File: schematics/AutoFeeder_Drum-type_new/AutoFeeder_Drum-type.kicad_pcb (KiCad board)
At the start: 2 copper layers, 65.5 x 80 mm, 27 parts, among them J1 USB_C_Receptacle_6, J3 Conn_01x05, J4 Conn_02x02_Odd_Even, M1 Motor_DC, U2 NJL5901AR-1, U3 PIC16F1705-I/SO, U4 ZXBM5210-S, U6 NJL5901AR-1

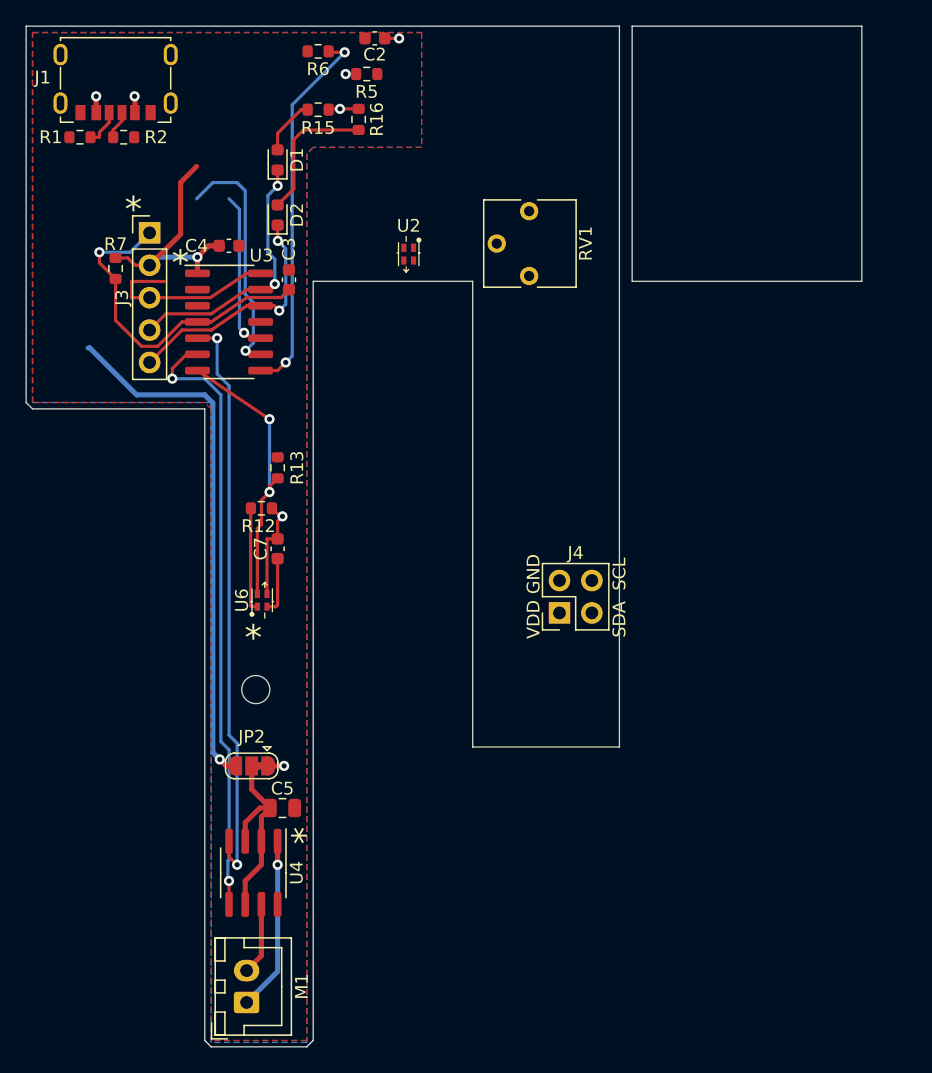
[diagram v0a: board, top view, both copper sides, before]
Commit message: Test reading/writing from/to HEF-block
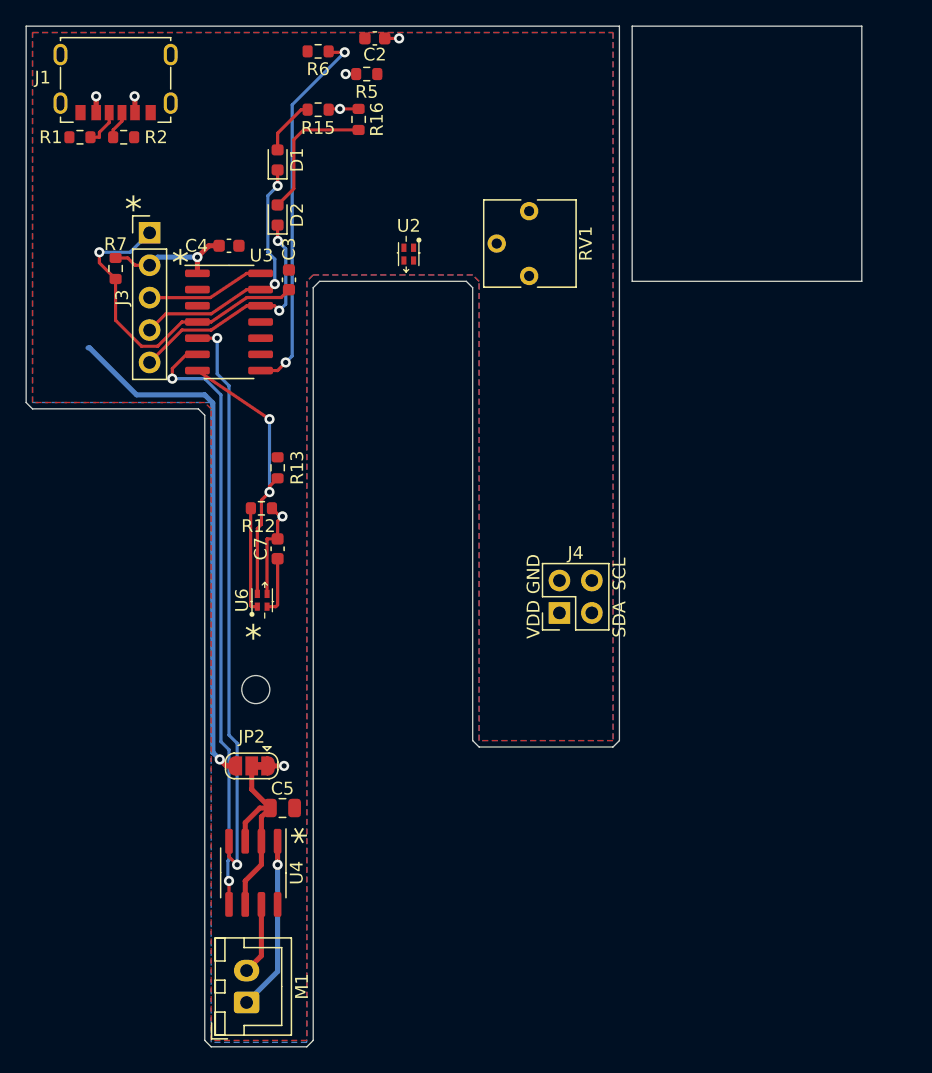
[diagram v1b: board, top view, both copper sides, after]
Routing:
- net /SDA: track 18.9 -> 0.00 mm, vias 1 -> 0
- net /SCL: track 12.4 -> 0.00 mm, vias 1 -> 0
- net +5V: track 35.8 -> 26.6 mm
- net GND: track 19.0 -> 13.8 mm
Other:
- outline, holes or cut-outs redrawn
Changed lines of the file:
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@@
     )
   )
-  (gr_line (start 137.16 81.28) (end 137.16 88.9) (layer "B.SilkS") (width 0.15))
-  (gr_line (start 137.16 88.9) (end 142.875 88.9) (layer "B.SilkS") (width 0.15))
-  (gr_line (start 142.875 81.28) (end 137.16 81.28) (layer "B.SilkS") (width 0.15))
-  (gr_line (start 142.875 88.9) (end 142.875 81.28) (layer "B.SilkS") (width 0.15))
   (gr_line (start 184 80) (end 184 60) (layer "Edge.Cuts") (width 0.1))
+  (gr_line (start 171.5 116) (end 172 116.5) (layer "Edge.Cuts") (width 0.1))
   (gr_line (start 136.5 60) (end 183 60) (layer "Edge.Cuts") (width 0.1))
-  (gr_line (start 171.5 80) (end 171.5 116.5) (layer "Edge.Cuts") (width 0.1))
-  (gr_line (start 183 60) (end 183 116.5) (layer "Edge.Cuts") (width 0.1))
-  (gr_line (start 159 80) (end 159 139.5) (layer "Edge.Cuts") (width 0.1))
-  (gr_line (start 137 90) (end 150.5 90) (layer "Edge.Cuts") (width 0.1))
-  (gr_line (start 171.5 80) (end 159 80) (layer "Edge.Cuts") (width 0.1))
+  (gr_line (start 171.5 80.5) (end 171.5 116) (layer "Edge.Cuts") (width 0.1))
+  (gr_line (start 183 60) (end 183 116) (layer "Edge.Cuts") (width 0.1))
+  (gr_line (start 159 80.5) (end 159 139.5) (layer "Edge.Cuts") (width 0.1))
+  (gr_line (start 171 80) (end 171.5 80.5) (layer "Edge.Cuts") (width 0.1))
+  (gr_line (start 137 90) (end 150 90) (layer "Edge.Cuts") (width 0.1))
+  (gr_line (start 171 80) (end 159.5 80) (layer "Edge.Cuts") (width 0.1))
   (gr_line (start 150.5 139.5) (end 151 140) (layer "Edge.Cuts") (width 0.1))
   (gr_line (start 202 60) (end 202 80) (layer "Edge.Cuts") (width 0.1))
@@
   (gr_line (start 151 140) (end 158.5 140) (layer "Edge.Cuts") (width 0.1))
   (gr_line (start 202 80) (end 184 80) (layer "Edge.Cuts") (width 0.1))
-  (gr_line (start 150.5 90) (end 150.5 139.5) (layer "Edge.Cuts") (width 0.1))
+  (gr_line (start 150 90) (end 150.5 90.5) (layer "Edge.Cuts") (width 0.1))
+  (gr_line (start 150.5 90.5) (end 150.5 139.5) (layer "Edge.Cuts") (width 0.1))
+  (gr_line (start 159.5 80) (end 159 80.5) (layer "Edge.Cuts") (width 0.1))
   (gr_line (start 136.5 89.5) (end 137 90) (layer "Edge.Cuts") (width 0.1))
-  (gr_line (start 171.5 116.5) (end 183 116.5) (layer "Edge.Cuts") (width 0.1))
+  (gr_line (start 172 116.5) (end 182.5 116.5) (layer "Edge.Cuts") (width 0.1))
   (gr_line (start 184 60) (end 202 60) (layer "Edge.Cuts") (width 0.1))
   (gr_line (start 136.5 60) (end 136.5 89.5) (layer "Edge.Cuts") (width 0.1))
+  (gr_line (start 182.5 116.5) (end 183 116) (layer "Edge.Cuts") (width 0.1))
   (gr_text "GND" (at 147.32 81.28) (layer "B.SilkS")
     (effects (font (size 1 1) (thickness 0.15)) (justify right mirror))
@@
     (style (thickness 0.15) (arrow_length 1.27) (text_position_mode 0) (extension_height 0.58642) (extension_offset 0.5) keep_text_aligned)
   )
-  (segment (start 144.78 81.28) (end 144.78 80.01) (width 0.25) (layer "F.Cu") (net 1))
   (segment (start 150.936751 81.28) (end 153.797 79.375) (width 0.25) (layer "F.Cu") (net 1))
-  (segment (start 144.78 80.01) (end 147.32 80.01) (width 0.25) (layer "F.Cu") (net 1))
   (segment (start 156.0675 105.5) (end 156.21 105.3575) (width 0.25) (layer "F.Cu") (net 1))
-  (segment (start 146.177 81.28) (end 144.78 81.28) (width 0.25) (layer "F.Cu") (net 1))
   (segment (start 155.38 105.5) (end 156.0675 105.5) (width 0.25) (layer "F.Cu") (net 1))
   (segment (start 153.797 79.375) (end 154.875 79.375) (width 0.25) (layer "F.Cu") (net 1))
@@
   (segment (start 156.4 98.425) (end 155.765 97.79) (width 0.25) (layer "F.Cu") (net 2))
   (segment (start 156.718 117.983) (end 155.478 117.983) (width 0.4) (layer "F.Cu") (net 2))
-  (segment (start 146.177 78.74) (end 148.61 76.307) (width 0.4) (layer "F.Cu") (net 2))
   (segment (start 144.463 78.169) (end 145.034 78.74) (width 0.25) (layer "F.Cu") (net 2))
   (segment (start 160.273 66.485) (end 160.21 66.548) (width 0.25) (layer "F.Cu") (net 2))
   (segment (start 156.591 98.425) (end 156.4 98.425) (width 0.25) (layer "F.Cu") (net 2))
-  (segment (start 148.61 72.243) (end 149.86 70.993) (width 0.4) (layer "F.Cu") (net 2))
   (segment (start 145 65.5) (end 145.03 65.53) (width 0.4) (layer "F.Cu") (net 2))
   (segment (start 156.21 100.19) (end 155.38 100.19) (width 0.25) (layer "F.Cu") (net 2))
   (segment (start 145.034 78.74) (end 146.177 78.74) (width 0.25) (layer "F.Cu") (net 2))
   (segment (start 155.38 100.19) (end 155.38 104.5) (width 0.25) (layer "F.Cu") (net 2))
-  (segment (start 148.61 76.307) (end 148.61 72.243) (width 0.4) (layer "F.Cu") (net 2))
   (segment (start 149.925 78.105) (end 149.925 79.375) (width 0.4) (layer "F.Cu") (net 2))
   (segment (start 156.591 98.425) (end 156.21 98.806) (width 0.25) (layer "F.Cu") (net 2))
@@
   (segment (start 152.4005 116.7135) (end 152.4005 125.339195) (width 0.25) (layer "B.Cu") (net 11))
   (segment (start 151.765 116.078) (end 152.4005 116.7135) (width 0.25) (layer "B.Cu") (net 11))
-  (segment (start 153.580202 84.036798) (end 154.051 84.455) (width 0.25) (layer "F.Cu") (net 12))
-  (segment (start 154.051 84.455) (end 154.875 84.455) (width 0.25) (layer "F.Cu") (net 12))
-  (via (at 153.580202 84.036798) (size 0.8) (drill 0.4) (layers "F.Cu" "B.Cu") (net 12))
-  (segment (start 153.22 83.676596) (end 153.580202 84.036798) (width 0.25) (layer "B.Cu") (net 12))
-  (segment (start 153.22 74.353) (end 153.22 83.676596) (width 0.25) (layer "B.Cu") (net 12))
-  (segment (start 152.4 73.533) (end 153.22 74.353) (width 0.25) (layer "B.Cu") (net 12))
-  (segment (start 154.137896 85.725) (end 154.875 85.725) (width 0.25) (layer "F.Cu") (net 13))
-  (segment (start 153.697836 85.443164) (end 154.137896 85.725) (width 0.25) (layer "F.Cu") (net 13))
-  (via (at 153.697836 85.443164) (size 0.8) (drill 0.4) (layers "F.Cu" "B.Cu") (net 13))
-  (segment (start 154.305202 84.835798) (end 154.305202 81.661202) (width 0.25) (layer "B.Cu") (net 13))
-  (segment (start 153.67 81.026) (end 153.67 72.898) (width 0.25) (layer "B.Cu") (net 13))
-  (segment (start 153.035 72.263) (end 151.13 72.263) (width 0.25) (layer "B.Cu") (net 13))
-  (segment (start 153.67 72.898) (end 153.035 72.263) (width 0.25) (layer "B.Cu") (net 13))
-  (segment (start 153.697836 85.443164) (end 154.305202 84.835798) (width 0.25) (layer "B.Cu") (net 13))
-  (segment (start 154.305202 81.661202) (end 153.67 81.026) (width 0.25) (layer "B.Cu") (net 13))
-  (segment (start 151.13 72.263) (end 149.86 73.533) (width 0.25) (layer "B.Cu") (net 13))
   (segment (start 154.095 97.81) (end 154.115 97.79) (width 0.25) (layer "F.Cu") (net 14))
   (segment (start 154.095 105.41) (end 154.095 97.81) (width 0.25) (layer "F.Cu") (net 14))
@@
     (connect_pads (clearance 0.508))
     (min_thickness 0.254) (filled_areas_thickness no)
-    (fill yes (thermal_gap 0.508) (thermal_bridge_width 0.508))
+    (fill (thermal_gap 0.508) (thermal_bridge_width 0.508))
     (polygon
       (pts
-        (xy 167.5 69.5)
-        (xy 159 69.5)
-        (xy 158.5 70)
+        (xy 182.5 116)
+        (xy 172 116)
+        (xy 172 80)
+        (xy 171.5 79.5)
+        (xy 159 79.5)
+        (xy 158.5 80)
         (xy 158.5 139.5)
         (xy 151 139.5)
@@
         (xy 137 89.5)
         (xy 137 60.5)
-        (xy 167.5 60.5)
+        (xy 182.5 60.5)
       )
     )
@@
     (connect_pads (clearance 0.508))
     (min_thickness 0.254) (filled_areas_thickness no)
-    (fill yes (thermal_gap 0.508) (thermal_bridge_width 0.508))
+    (fill (thermal_gap 0.508) (thermal_bridge_width 0.508))
     (polygon
       (pts
-        (xy 167.5 69.5)
-        (xy 159 69.5)
-        (xy 158.5 70)
+        (xy 182.5 116)
+        (xy 172 116)
+        (xy 172 80)
+        (xy 171.5 79.5)
+        (xy 159 79.5)
+        (xy 158.5 80)
         (xy 158.5 139.65)
         (xy 151 139.65)
@@
         (xy 137 89.5)
         (xy 137 60.5)
-        (xy 167.5 60.5)
+        (xy 182.5 60.5)
       )
     )

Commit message: Rev.02: Rev01 had a problem with the deep feeder hitting the PCB. Rev02 avoided this problem by overlapping two PCBs for the sensor section.; Three sensitivity options are available for white, transparent, and black feeders.
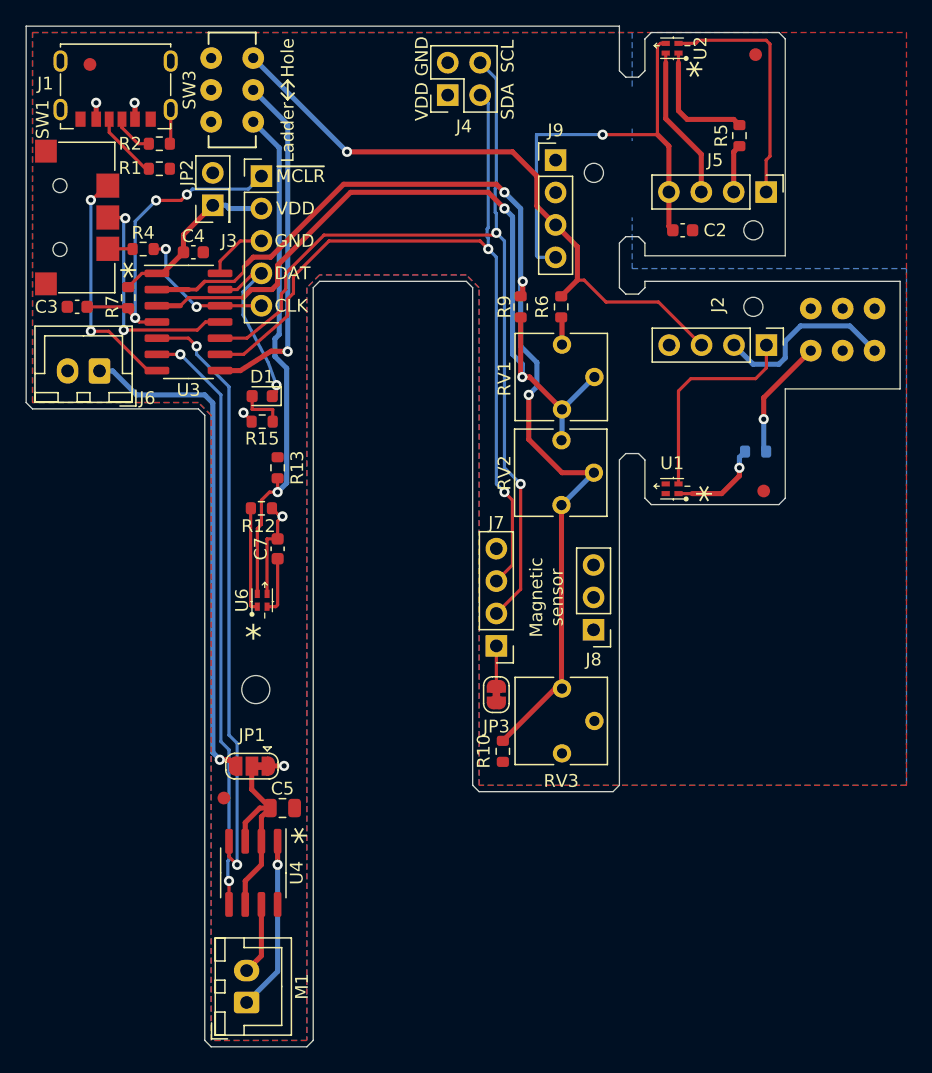
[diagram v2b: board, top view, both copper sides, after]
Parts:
- removed D2: LED, LED_SMD:LED_0603_1608Metric
- removed R16: 1k, Resistor_SMD:R_0603_1608Metric
- added ?: , , F.Cu at (194.3, 96.4)
- added ?: , , F.Cu at (193.7, 62.2)
- added ?: , , F.Cu at (141.5, 63.0)
- added J2: Conn_01x04, Connector_PinHeader_2.54mm:PinHeader_1x04_P2.54mm_Vertical, F.Cu at (194.5, 85.0)
- added J5: Conn_01x04, Connector_PinHeader_2.54mm:PinHeader_1x04_P2.54mm_Vertical, F.Cu at (194.5, 73.0)
- added J6: Conn_01x02, Connector_JST:JST_XH_B2B-XH-A_1x02_P2.50mm_Vertical, F.Cu at (142.2, 87.0)
- added J7: Conn_01x04, Connector_PinHeader_2.54mm:PinHeader_1x04_P2.54mm_Vertical, F.Cu at (173.4, 108.6)
- added J8: Conn_01x03, Connector_PinHeader_2.54mm:PinHeader_1x03_P2.54mm_Vertical, F.Cu at (181.0, 107.3)
- added J9: Conn_01x04, Connector_PinHeader_2.54mm:PinHeader_1x04_P2.54mm_Vertical, F.Cu at (178.0, 70.5)
- added JP1: SolderJumper, Jumper:SolderJumper-3_P1.3mm_Bridged12_RoundedPad1.0x1.5mm, F.Cu at (154.2, 118.0)
- added JP3: Jumper_2_Bridged, Jumper:SolderJumper-2_P1.3mm_Bridged_RoundedPad1.0x1.5mm, F.Cu at (173.4, 112.4)
- added R10: 18k, Resistor_SMD:R_0603_1608Metric, F.Cu at (173.9, 116.8)
- added R4: 1k, Resistor_SMD:R_0603_1608Metric, F.Cu at (145.7, 77.5)
- added R8: 510, Resistor_SMD:R_0603_1608Metric, B.Cu at (193.7, 93.3)
- added R9: 10k, Resistor_SMD:R_0603_1608Metric, F.Cu at (175.3, 82.0)
- added REF**: DrillHoleOval2x2, mylib:DrillHoleOval2.5x8mm, F.Cu at (181.0, 71.5)
- added REF**: DrillHoleOval2x2, mylib:DrillHoleOval2.5x8mm, F.Cu at (193.5, 76.0)
- added REF**: DrillHoleOval2x4, mylib:DrillHoleOval2.5x8mm, F.Cu at (170.0, 75.0)
- added REF**: DrillHoleOval2x6, mylib:DrillHoleOval2.5x8mm, F.Cu at (184.0, 85.0)
- added REF**: DrillHoleOval2x4, mylib:DrillHoleOval2.5x8mm, F.Cu at (184.0, 66.5)
- added REF**: DrillHoleOval2x4, mylib:DrillHoleOval2.5x8mm, F.Cu at (190.5, 65.0)
- added REF**: Fiducial_1mm_Mask2mm, Fiducial:Fiducial_1mm_Mask2mm, F.Cu at (152.0, 120.5)
- added REF**: DrillHoleOval2x6, mylib:DrillHoleOval2.5x8mm, F.Cu at (190.0, 92.7)
- added REF**: DrillHoleOval2x2, mylib:DrillHoleOval2.5x8mm, F.Cu at (193.5, 82.0)
- added REF**: DrillHoleOval2.5x8mm, mylib:DrillHoleOval2.5x8mm, F.Cu at (184.0, 72.0)
- added REF**: DrillHoleOval2x3, mylib:DrillHoleOval2.5x8mm, F.Cu at (184.0, 91.0)
- added RV2: 20k, Potentiometer_THT:Potentiometer_Vishay_T73YP_Vertical, F.Cu at (178.5, 97.5)
- added RV3: 20k, Potentiometer_THT:Potentiometer_Vishay_T73YP_Vertical, F.Cu at (178.5, 117.0)
- added SW1: SW_SPDT_AND_Push, mylib:THMU26_2, F.Cu at (139.3, 75.0)
- added SW2: IS-2235, mylib:Slide-SW-IS-2235, B.Cu at (198.0, 85.4)
- added SW3: IS-2235, mylib:Slide-SW-IS-2235, F.Cu at (154.3, 62.5)
- added U1: NJL5901AR-1, mylib:NJL5901AR-1, F.Cu at (187.1, 96.3)
- JP2: value SolderJumper -> Jumper_2_Bridged; footprint Jumper:SolderJumper-3_P1.3mm_Bridged12_RoundedPad1.0x1.5mm -> Connector_PinHeader_2.54mm:PinHeader_2x01_P2.54mm_Vertical
- R5: value 820 -> 510
- RV1: value 50k -> 1k
- moved JP2 44.0 mm to (151.1, 74.0), turned to 90 degrees
- moved J4 41.5 mm to (169.5, 65.4)
- moved R5 29.6 mm to (192.4, 68.6), turned to 90 degrees
- moved C2 28.4 mm to (188.0, 76.0), turned to 0 degrees
- moved R6 27.6 mm to (178.4, 82.0), turned to -90 degrees
- moved U2 26.2 mm to (187.1, 61.7), turned to 0 degrees
- moved R15 24.8 mm to (155.0, 91.0), turned to 0 degrees
- moved D1 18.6 mm to (155.0, 89.0), turned to 180 degrees
- moved C3 16.7 mm to (140.5, 82.0), turned to 180 degrees
- moved RV1 15.8 mm to (178.5, 90.0), turned to 0 degrees
- moved J3 9.83 mm to (154.9, 71.8)
- moved R1 6.69 mm to (146.9, 71.2), turned to 0 degrees
- moved U3 3.18 mm to (149.2, 83.2)
- moved C4 2.84 mm to (149.6, 77.7)
- moved R2 2.84 mm to (146.9, 69.2)
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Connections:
- net Net-(D2-Pad1) renamed /CCW
- C4 pad 2: +5V -> Net-(C4-Pad2)
- J3 pad 2: +5V -> Net-(C4-Pad2)
- JP2 pad 1: +5V -> Net-(C4-Pad2)
- JP2 pad 2: Net-(C5-Pad1) -> +5V
- R5 pad 1: +5V -> /IR_DOWN
- R7 pad 2: +5V -> Net-(C4-Pad2)
- RV1 pad 1: Net-(R6-Pad2) -> /RA4
- RV1 pad 2: GND -> /RA4
- RV1 pad 3: GND -> Net-(R6-Pad2)
- U2 pad 4: /Sensor0 -> Net-(J5-Pad3)
- U3 pad 1: +5V -> Net-(C4-Pad2)
- U3 pad 2: /Sw1 -> /RA5
- U3 pad 7: /Sensor1 -> /CW
- U3 pad 8: /Sensor0 -> Net-(SW3-Pad2)
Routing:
- net /RA5: track 0.00 -> 83.7 mm, vias 0 -> 3
- net /SCL: track 0.00 -> 71.8 mm, vias 0 -> 2
- net /SDA: track 0.00 -> 66.1 mm, vias 0 -> 2
- net /RA4: track 0.00 -> 61.0 mm, vias 0 -> 2
- net /VM: track 41.1 -> 0.00 mm, vias 1 -> 0
- net Net-(J6-Pad1): track 0.00 -> 39.5 mm, vias 0 -> 1
- net GND: track 13.8 -> 47.9 mm
- net Net-(SW3-Pad2): track 0.00 -> 27.4 mm, vias 0 -> 1
- net +5V: track 26.6 -> 49.2 mm, vias 8 -> 6
- net /Sensor0: track 29.7 -> 49.2 mm, vias 2 -> 1
- net /CW: track 0.00 -> 18.6 mm, vias 0 -> 2
- net /Sensor1: track 22.2 -> 40.8 mm, vias 2 -> 1
- net /RA2: track 0.00 -> 18.0 mm, vias 0 -> 2
- net Net-(J2-Pad2): track 0.00 -> 14.4 mm
- net Net-(C4-Pad2): track 0.00 -> 14.0 mm
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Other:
- board size 65.5 x 80 mm -> 68.5 x 80 mm
- board text added: "0.25mm Not required"
- board text added: "Hole"
- board text added: "Ladder"
- board text added: "Lower"
- board text added: "Magnetic sensor"
- board text added: "Rev.02 * Add Fiducals * Add holes, labels, etc."
- board text added: "Upper"
- board text added: "n.k products 2024 Auto Feeder Rev.02"
- board text removed: "n.k products 2023 Auto Feeder Rev.01"

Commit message: Change Schematics; Add Red LED for ladder sensor; Add guide line of feeder tape
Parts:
- added D2: LED, LED_SMD:LED_0603_1608Metric, F.Cu at (158.0, 67.0)
- JP3: value Jumper_2_Bridged -> SolderJumper_3_Bridged12; footprint Jumper:SolderJumper-2_P1.3mm_Bridged_RoundedPad1.0x1.5mm -> Jumper:SolderJumper-3_P1.3mm_Bridged12_RoundedPad1.0x1.5mm; moved to B.Cu
- SW1: value SW_SPDT_AND_Push -> TMHU26
- moved D1 26.2 mm to (158.0, 63.0), turned to -90 degrees
- moved R15 21.6 mm to (158.2, 69.6), turned to 180 degrees
- moved JP3 5.01 mm to (176.5, 108.5)
- moved ? 1.80 mm to (194.0, 64.0)
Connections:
- D1 pad 1: Net-(D1-Pad1) -> Net-(SW3-Pad4)
- J3 pad 4: Net-(D1-Pad1) -> Net-(J3-Pad4)
- SW3 pad 4: unconnected-(SW3-Pad4) -> Net-(SW3-Pad4)
- SW3 pad 5: unconnected-(SW3-Pad5) -> Net-(J3-Pad4)
- SW3 pad 6: unconnected-(SW3-Pad6) -> Net-(SW3-Pad6)
- U3 pad 13: Net-(D1-Pad1) -> Net-(J3-Pad4)
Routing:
- net GND: track 47.9 -> 72.4 mm, vias 0 -> 1
- net Net-(J3-Pad4): track 0.00 -> 21.5 mm
- net Net-(D1-Pad1): track 14.7 -> 0.00 mm, vias 1 -> 0
- net Net-(SW3-Pad4): track 0.00 -> 8.22 mm
- net Net-(SW3-Pad6): track 0.00 -> 7.53 mm
- net /Sensor0: track 49.2 -> 53.5 mm
- net Net-(D1-Pad2): track 3.62 -> 6.88 mm
